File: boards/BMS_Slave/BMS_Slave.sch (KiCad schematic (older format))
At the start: 63 parts, among them J1 Mounting_Hole_4-40, J2 Mounting_Hole_4-40, J3 Mounting_Hole_4-40, J4 Mounting_Hole_4-40, J5 MicroFit_12, J6 MicroFit_20, J7 NanoFit_2, J8 NanoFit_2, Q1 Q_NPN_BCE, T1 T_LAN_7490100111A, U1 LTC6811-1, U2 24AA01, U3 MCP6001, U4 LTC1380, U5 LTC1380, U6 MCP6001

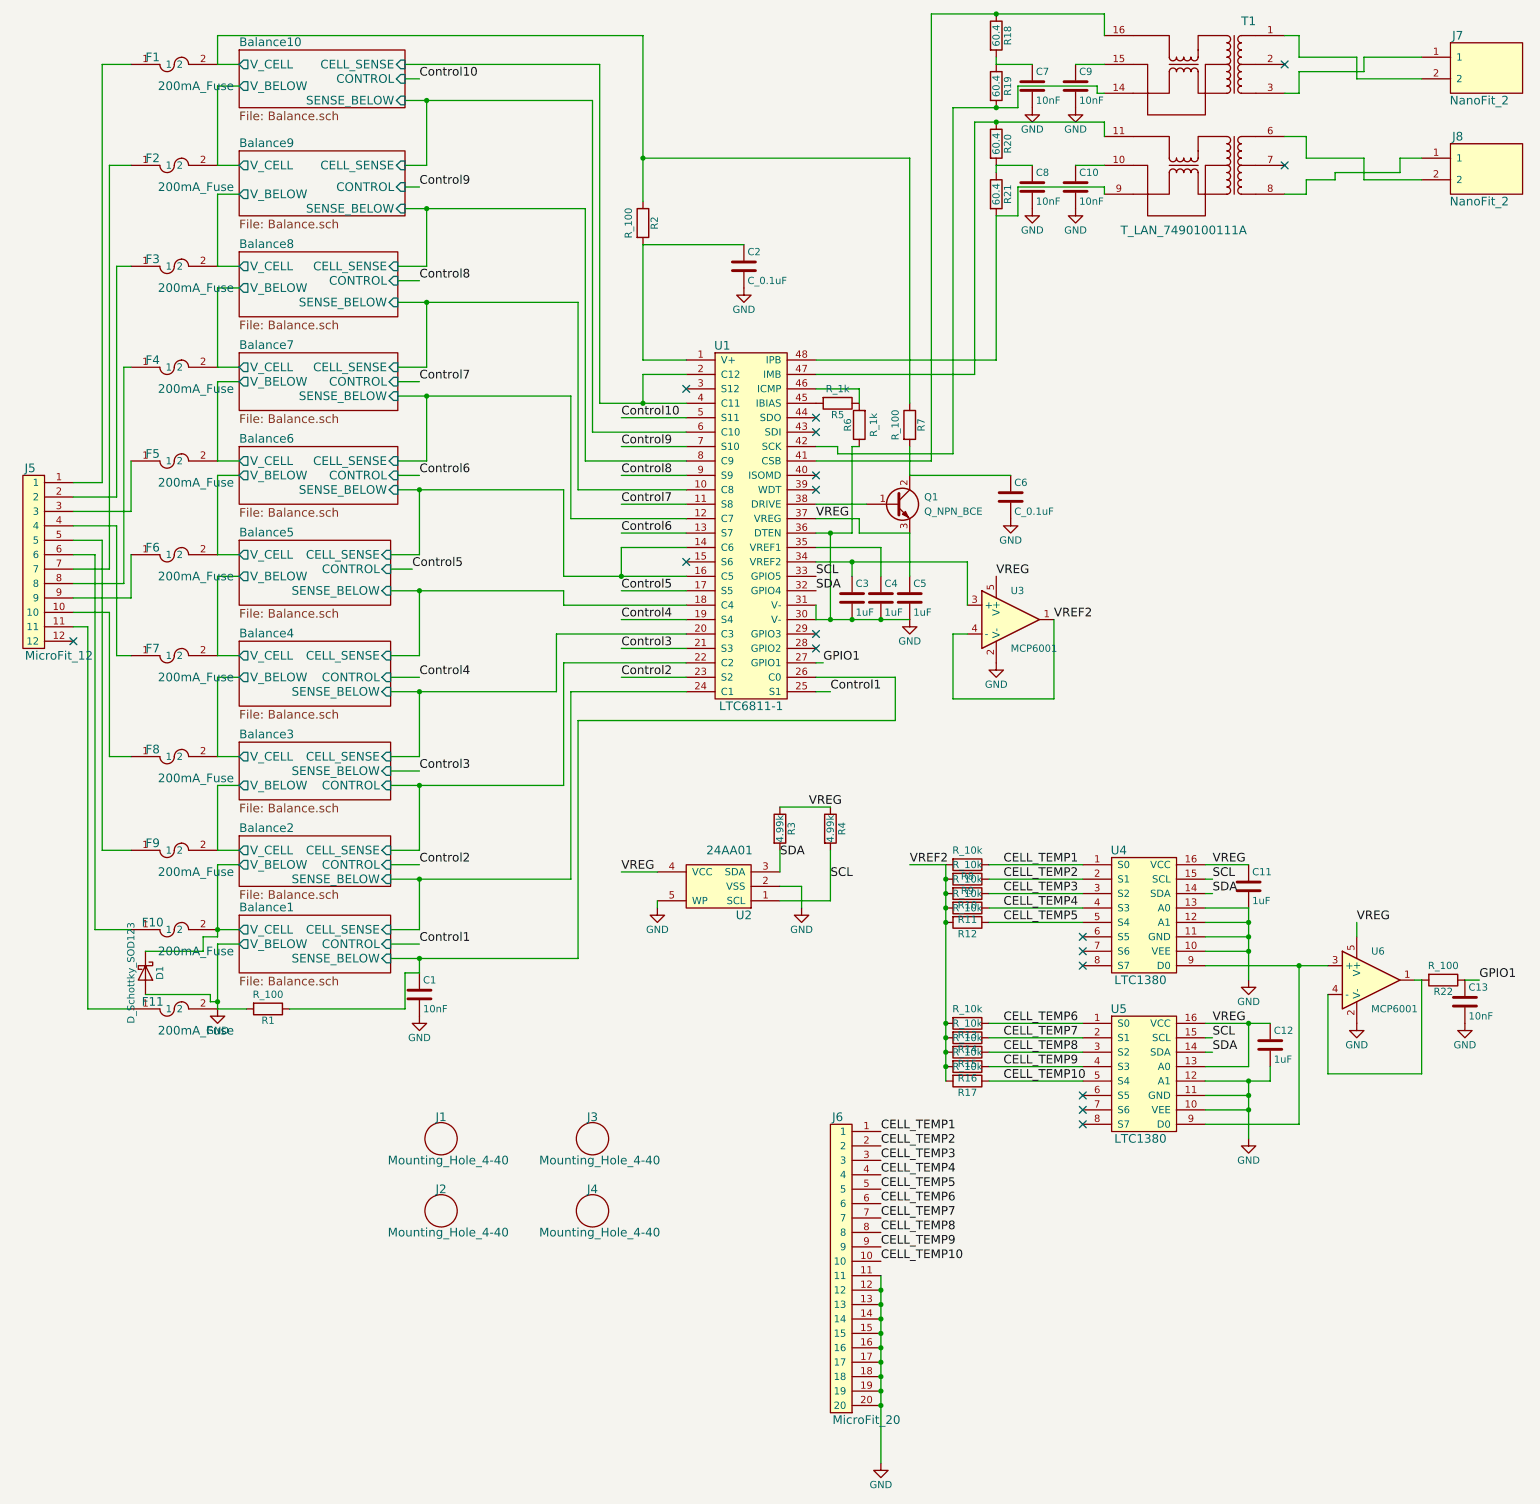
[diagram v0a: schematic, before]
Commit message: BMS_Slave: Fixed routing for microfits
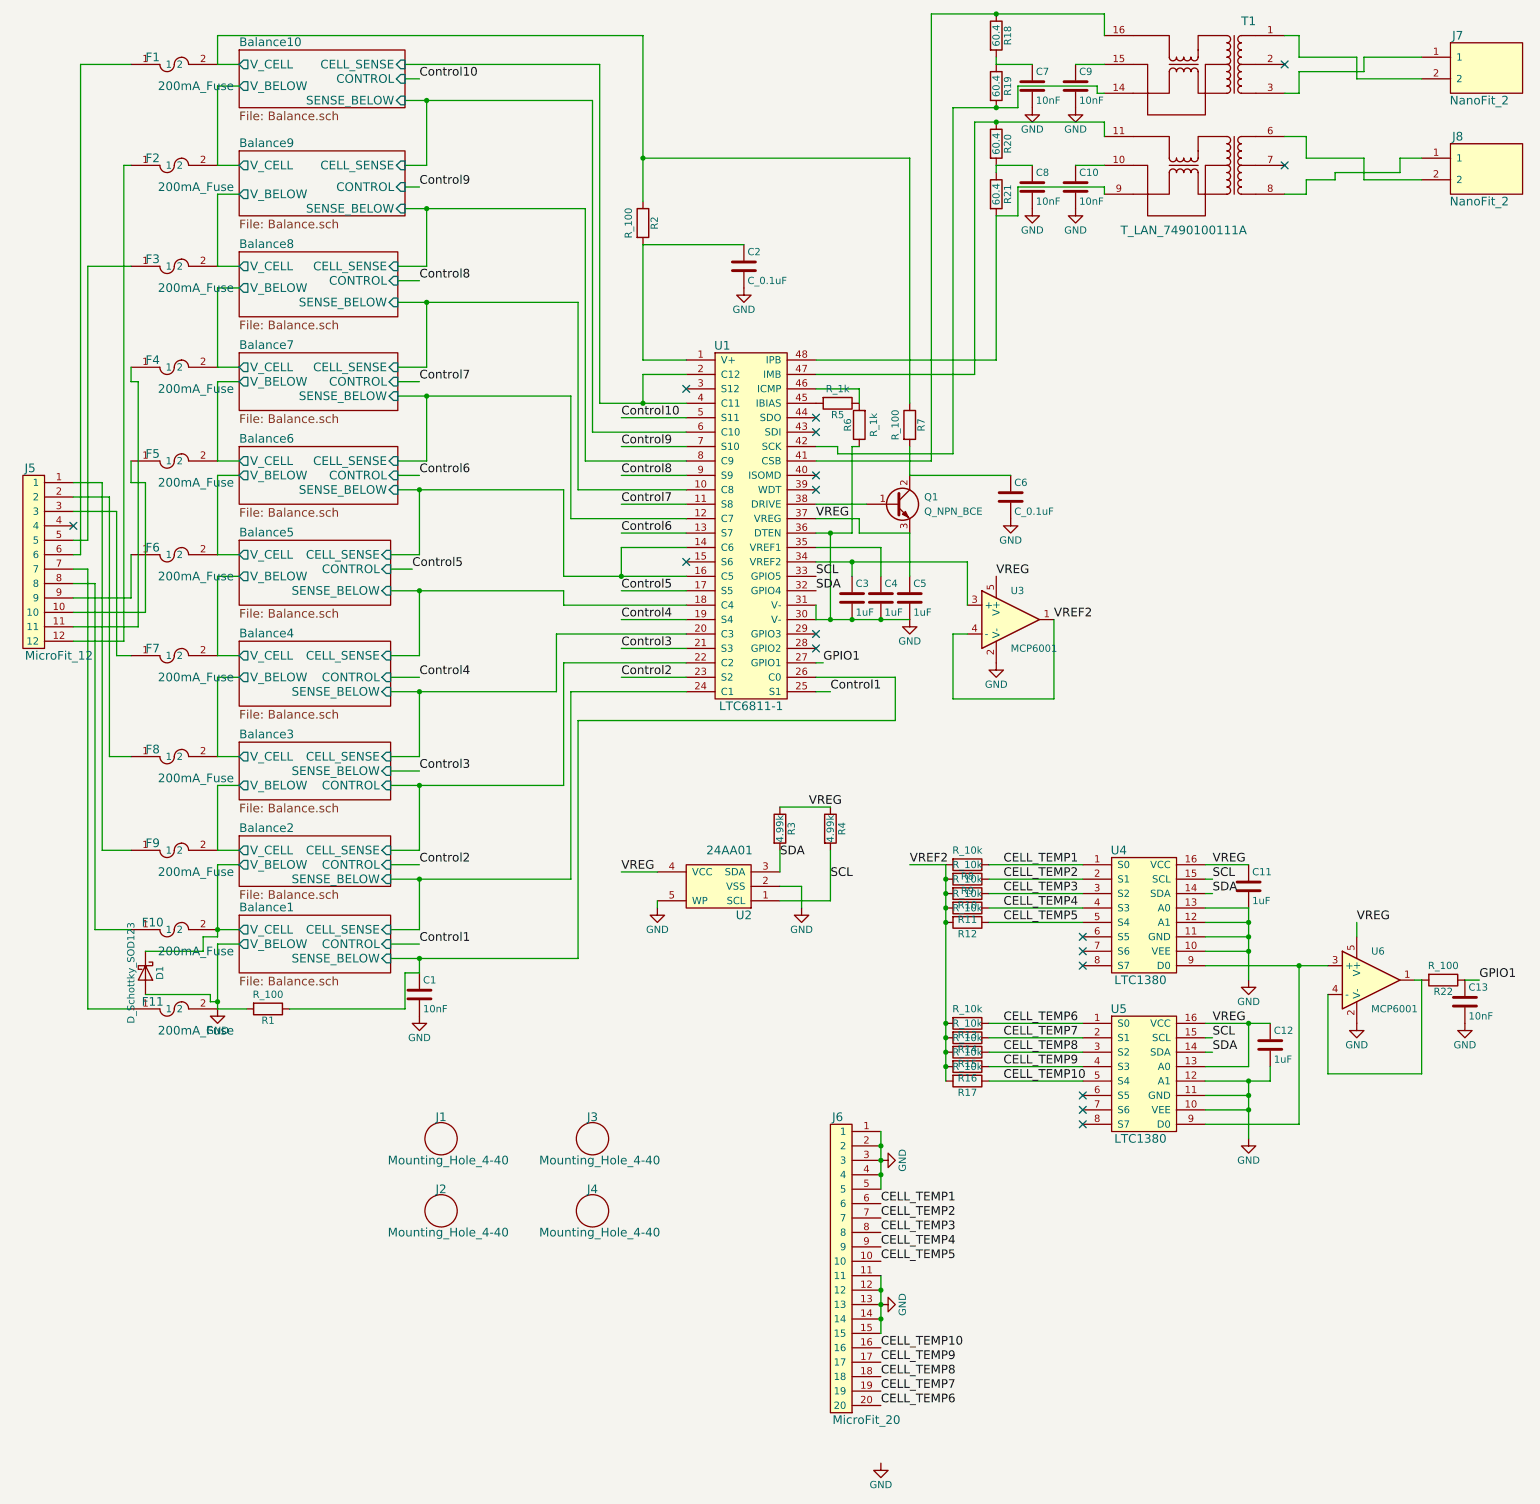
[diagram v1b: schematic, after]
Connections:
- net CELL_TEMP1: now also J6.6; no longer J6.1
- net CELL_TEMP10: now also J6.16; no longer J6.10
- net CELL_TEMP2: now also J6.7; no longer J6.2
- net CELL_TEMP3: now also J6.8; no longer J6.3
- net CELL_TEMP4: now also J6.9; no longer J6.4
- net CELL_TEMP5: now also J6.10; no longer J6.5
- net CELL_TEMP6: now also J6.20; no longer J6.6
- net CELL_TEMP7: now also J6.19; no longer J6.7
- net CELL_TEMP8: now also J6.18; no longer J6.8
- net CELL_TEMP9: now also J6.17; no longer J6.9
- net GND: now also J6.1, J6.2, J6.3, J6.4, J6.5; no longer J6.16, J6.17, J6.18, J6.19, J6.20
- net at F1.1: now also J5.6; no longer J5.1
- net at F2.1: now also J5.12; no longer J5.7
- net at F3.1: now also J5.5; no longer J5.2
- net at F4.1: now also J5.11; no longer J5.8
- net at F5.1: now also J5.10; no longer J5.3
- net at F7.1: now also J5.3; no longer J5.4
- net at F8.1: now also J5.2; no longer J5.10
- net at F9.1: now also J5.1; no longer J5.5
- net at F10.1: now also J5.8; no longer J5.6
- net at F11.1: now also J5.7; no longer J5.11
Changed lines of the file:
@@
 	1    0    0    -1
 $EndComp
-Text Label 6400 8350 0    60   ~ 0
+Text Label 6400 8850 0    60   ~ 0
 CELL_TEMP1
-Text Label 6400 8450 0    60   ~ 0
+Text Label 6400 8950 0    60   ~ 0
 CELL_TEMP2
-Text Label 6400 8550 0    60   ~ 0
+Text Label 6400 9050 0    60   ~ 0
 CELL_TEMP3
-Text Label 6400 8650 0    60   ~ 0
+Text Label 6400 9150 0    60   ~ 0
 CELL_TEMP4
-Text Label 6400 8750 0    60   ~ 0
+Text Label 6400 9250 0    60   ~ 0
 CELL_TEMP5
-Text Label 6400 8850 0    60   ~ 0
+Text Label 6400 10250 0    60   ~ 0
 CELL_TEMP6
-Text Label 6400 8950 0    60   ~ 0
+Text Label 6400 10150 0    60   ~ 0
 CELL_TEMP7
-Text Label 6400 9050 0    60   ~ 0
+Text Label 6400 10050 0    60   ~ 0
 CELL_TEMP8
-Text Label 6400 9150 0    60   ~ 0
+Text Label 6400 9950 0    60   ~ 0
 CELL_TEMP9
-Text Label 6400 9250 0    60   ~ 0
+Text Label 6400 9850 0    60   ~ 0
 CELL_TEMP10
 $Comp
@@
 	1    0    0    -1
 $EndComp
-NoConn ~ 800  4950
 Wire Wire Line
 	1800 750  4750 750
@@
 	900  7500 1200 7500
 Wire Wire Line
-	1150 4550 1150 3050
-Wire Wire Line
-	1150 3050 1200 3050
-Wire Wire Line
-	1100 2350 1200 2350
-Wire Wire Line
-	1050 4450 1050 1650
-Wire Wire Line
-	1050 1650 1200 1650
-Wire Wire Line
-	1000 3850 1000 950
-Wire Wire Line
-	1000 950  1200 950
+	850  950  1200 950
+Wire Wire Line
+	6300 4000 5950 4000
+Wire Wire Line
+	9350 1600 9750 1600
+Wire Wire Line
+	9750 1600 9750 1750
+Wire Wire Line
+	9750 1750 10150 1750
+Wire Wire Line
+	9350 1750 9550 1750
+Wire Wire Line
+	9550 1750 9550 1700
+Wire Wire Line
+	9550 1700 10000 1700
+Wire Wire Line
+	10000 1700 10000 1600
+Wire Wire Line
+	10000 1600 10150 1600
+Wire Wire Line
+	9300 900  9700 900
+Wire Wire Line
+	9700 900  9700 1050
+Wire Wire Line
+	9700 1050 10150 1050
+Wire Wire Line
+	9300 1000 9750 1000
+Wire Wire Line
+	9750 1000 9750 900
+Wire Wire Line
+	9750 900  10150 900
+Wire Wire Line
+	1100 5050 1200 5050
+Wire Wire Line
+	1100 4050 1100 5050
+Wire Wire Line
+	1050 3950 1050 5750
+Wire Wire Line
+	1000 3850 1000 6400
+Wire Wire Line
+	6400 8350 6400 8750
+Connection ~ 6400 8650
+Connection ~ 6400 8550
+Connection ~ 6400 8450
+Wire Wire Line
+	6400 9350 6400 9750
+Connection ~ 6400 9650
+Connection ~ 6400 9550
 Connection ~ 6400 9450
-Connection ~ 6400 9550
-Connection ~ 6400 9650
-Connection ~ 6400 9750
-Connection ~ 6400 9850
-Connection ~ 6400 9950
-Connection ~ 6400 10050
-Connection ~ 6400 10150
-Connection ~ 6400 10250
-Wire Wire Line
-	6300 4000 5950 4000
-Wire Wire Line
-	6400 9350 6400 10650
-Wire Wire Line
-	9350 1600 9750 1600
-Wire Wire Line
-	9750 1600 9750 1750
-Wire Wire Line
-	9750 1750 10150 1750
-Wire Wire Line
-	9350 1750 9550 1750
-Wire Wire Line
-	9550 1750 9550 1700
-Wire Wire Line
-	9550 1700 10000 1700
-Wire Wire Line
-	10000 1700 10000 1600
-Wire Wire Line
-	10000 1600 10150 1600
-Wire Wire Line
-	9300 900  9700 900
-Wire Wire Line
-	9700 900  9700 1050
-Wire Wire Line
-	9700 1050 10150 1050
-Wire Wire Line
-	9300 1000 9750 1000
-Wire Wire Line
-	9750 1000 9750 900
-Wire Wire Line
-	9750 900  10150 900
-Wire Wire Line
-	800  3850 1000 3850
-Wire Wire Line
-	800  4450 1050 4450
-Wire Wire Line
-	1100 3950 1100 2350
-Wire Wire Line
-	800  3950 1100 3950
-Wire Wire Line
-	800  4550 1150 4550
-Wire Wire Line
-	1200 4050 1200 3700
-Wire Wire Line
-	800  4050 1200 4050
-Wire Wire Line
-	1200 4650 1200 4350
-Wire Wire Line
-	800  4650 1200 4650
-Wire Wire Line
-	1200 5050 1100 5050
-Wire Wire Line
-	1100 5050 1100 4150
-Wire Wire Line
-	1100 4150 800  4150
-Wire Wire Line
-	1050 4750 1050 5750
-Wire Wire Line
-	800  4750 1050 4750
-Wire Wire Line
-	1000 4250 1000 6400
-Wire Wire Line
-	800  4250 1000 4250
-Wire Wire Line
-	950  6950 950  4350
-Wire Wire Line
-	950  4350 800  4350
-Wire Wire Line
-	900  7500 900  4850
-Wire Wire Line
-	900  4850 800  4850
+$Comp
+L GND #PWR018
+U 1 1 5A59223B
+P 6400 9550
+F 0 "#PWR018" H 6400 9300 50  0001 C CNN
+F 1 "GND" H 6400 9400 50  0000 C CNN
+F 2 "" H 6400 9550 50  0001 C CNN
+F 3 "" H 6400 9550 50  0001 C CNN
+	1    6400 9550
+	0    -1   -1   0
+$EndComp
+$Comp
+L GND #PWR019
+U 1 1 5A592700
+P 6400 8550
+F 0 "#PWR019" H 6400 8300 50  0001 C CNN
+F 1 "GND" H 6400 8400 50  0000 C CNN
+F 2 "" H 6400 8550 50  0001 C CNN
+F 3 "" H 6400 8550 50  0001 C CNN
+	1    6400 8550
+	0    -1   -1   0
+$EndComp
+Wire Wire Line
+	900  4450 900  7500
+Wire Wire Line
+	900  4450 800  4450
+Wire Wire Line
+	950  6950 950  4550
+Wire Wire Line
+	950  4550 800  4550
+Wire Wire Line
+	1000 3850 800  3850
+Wire Wire Line
+	1050 3950 800  3950
+Wire Wire Line
+	1100 4050 800  4050
+Wire Wire Line
+	800  4350 850  4350
+Wire Wire Line
+	850  4350 850  950
+Wire Wire Line
+	1150 4950 800  4950
+Wire Wire Line
+	1150 1650 1150 4950
+Wire Wire Line
+	1150 1650 1200 1650
+Wire Wire Line
+	800  4250 900  4250
+Wire Wire Line
+	900  4250 900  2350
+Wire Wire Line
+	900  2350 1200 2350
+Wire Wire Line
+	800  4850 1250 4850
+Wire Wire Line
+	1250 4850 1250 3150
+Wire Wire Line
+	1250 3150 1200 3150
+Wire Wire Line
+	1200 3150 1200 3050
+Wire Wire Line
+	1200 3700 1200 3850
+Wire Wire Line
+	1200 3850 1300 3850
+Wire Wire Line
+	1300 3850 1300 4750
+Wire Wire Line
+	1300 4750 800  4750
+Wire Wire Line
+	1200 4350 1200 4650
+Wire Wire Line
+	1200 4650 800  4650
+NoConn ~ 800  4150
 $EndSCHEMATC

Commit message: BMS: updating files
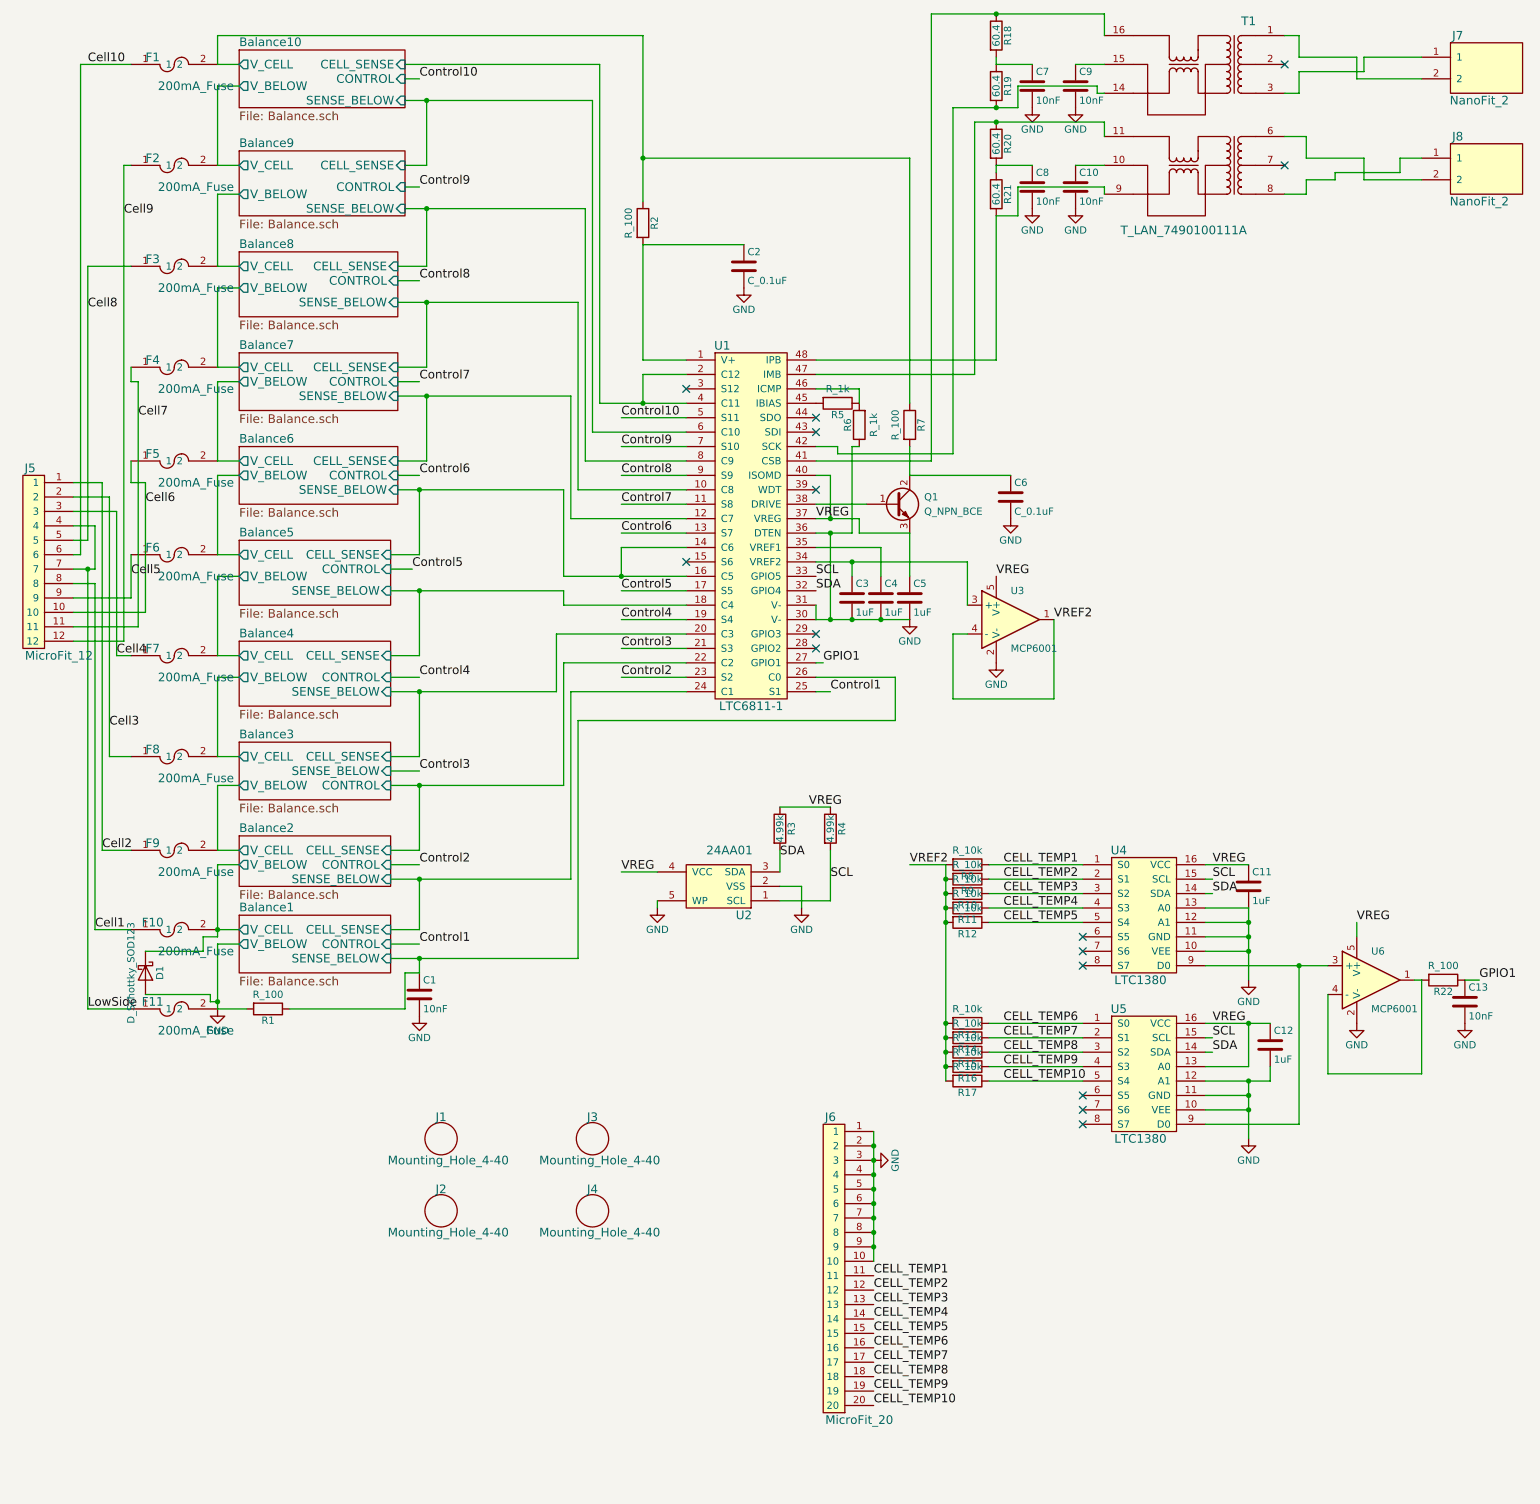
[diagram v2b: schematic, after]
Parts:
- J2, J4: footprint footprints:Mounting_Hole_4-40 -> footprints:Mounting_Hole_Insert_4-40
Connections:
- net CELL_TEMP1: now also J6.11; no longer J6.6
- net CELL_TEMP10: now also J6.20; no longer J6.16
- net CELL_TEMP2: now also J6.12; no longer J6.7
- net CELL_TEMP3: now also J6.13; no longer J6.8
- net CELL_TEMP4: now also J6.14; no longer J6.9
- net CELL_TEMP5: now also J6.15; no longer J6.10
- net CELL_TEMP6: now also J6.16; no longer J6.20
- net CELL_TEMP7: now also J6.17; no longer J6.19
- net CELL_TEMP9: now also J6.19; no longer J6.17
- net GND: now also J6.10, J6.6, J6.7, J6.8, J6.9; no longer J6.11, J6.12, J6.13, J6.14, J6.15
- net VREG: now also U1.40 (ISOMD)
- net Cell10: now reaches F1.1, J5.6
- net Cell9: now reaches F2.1, J5.12
- net Cell8: now reaches F3.1, J5.5
- net Cell7: now reaches F4.1, J5.11
- net Cell6: now reaches F5.1, J5.10
- net Cell5: now reaches F6.1, J5.9
- net Cell4: now reaches F7.1, J5.3
- net Cell3: now reaches F8.1, J5.2
- net Cell2: now reaches F9.1, J5.1
- net Cell1: now reaches F10.1, J5.8
- net LowSide: now reaches F11.1, J5.7
- net LowSide: now also J5.4
- no-connect marks 17 -> 15
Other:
- moved on the sheet: J6
